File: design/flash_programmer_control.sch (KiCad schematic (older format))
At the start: 10 parts, among them P601 ISP, U601 ATMEGA328P

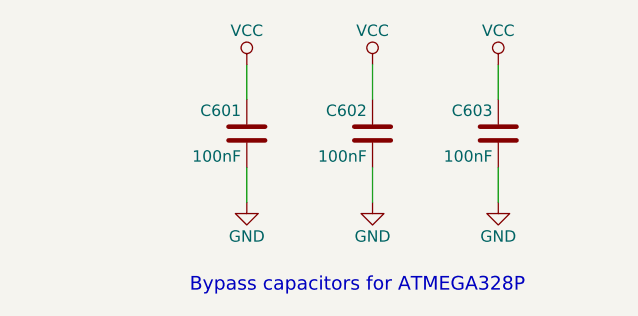
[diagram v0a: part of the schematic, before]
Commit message: Apply license to schematic files
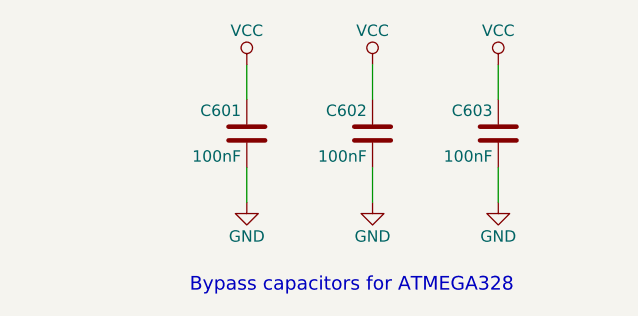
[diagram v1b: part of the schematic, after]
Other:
- note added: "Bypass capacitors for ATMEGA328"
- note removed: "Bypass capacitors for ATMEGA328P"
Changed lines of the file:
@@
 Date "2017-03-11"
 Rev "5"
-Comp "John DiSanti"
+Comp "Copyright 2017 John DiSanti"
 Comment1 ""
 Comment2 ""
@@
 	9500 6100 9500 6250
 Text Notes 8700 6650 0    60   ~ 0
-Bypass capacitors for ATMEGA328P
+Bypass capacitors for ATMEGA328
 $Comp
 L R R601

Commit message: Correction: ATMEGA328P -> ATMEGA328-AU
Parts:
- U601: value ATMEGA328P -> ATMEGA328-AU; symbol ATMEGA328P -> ATMEGA328-AU
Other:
- note added: "Bypass capacitors for ATMEGA328-AU"
- note removed: "Bypass capacitors for ATMEGA328"
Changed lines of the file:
@@
 EESchema Schematic File Version 2
 LIBS:gls27sf010
-LIBS:atmega328p
+LIBS:atmega328au
 LIBS:flash_programmer
 LIBS:power
@@
 	9500 6100 9500 6250
 Text Notes 8700 6650 0    60   ~ 0
-Bypass capacitors for ATMEGA328
+Bypass capacitors for ATMEGA328-AU
 $Comp
 L R R601
@@
 Control
 $Comp
-L ATMEGA328P U?
+L ATMEGA328-AU U?
 U 1 1 58C491ED
 P 3900 3550
@@
 AR Path="/58C243E5/58C491ED" Ref="U601"  Part="1"
 F 0 "U601" H 4100 3800 60  0000 L CNN
-F 1 "ATMEGA328P" H 4100 3700 60  0000 L CNN
+F 1 "ATMEGA328-AU" H 4100 3700 60  0000 L CNN
 F 2 "TQFP_32_7mm_0.8mm_pitch:TQFP-32" H 3900 3550 60  0001 C CNN
 F 3 "" H 3900 3550 60  0001 C CNN
@@
 $EndComp
 $Comp
-L ATMEGA328P U?
+L ATMEGA328-AU U?
 U 2 1 58C4927B
 P 7200 2150
@@
 AR Path="/58C243E5/58C4927B" Ref="U601"  Part="2"
 F 0 "U601" H 7400 2400 60  0000 L CNN
-F 1 "ATMEGA328P" H 7400 2300 60  0000 L CNN
+F 1 "ATMEGA328-AU" H 7400 2300 60  0000 L CNN
 F 2 "TQFP_32_7mm_0.8mm_pitch:TQFP-32" H 7200 2150 60  0001 C CNN
 F 3 "" H 7200 2150 60  0001 C CNN
@@
 $EndComp
 $Comp
-L ATMEGA328P U?
+L ATMEGA328-AU U?
 U 3 1 58C492C6
 P 3900 4200
@@
 AR Path="/58C243E5/58C492C6" Ref="U601"  Part="3"
 F 0 "U601" H 4100 4450 60  0000 L CNN
-F 1 "ATMEGA328P" H 4100 4350 60  0000 L CNN
+F 1 "ATMEGA328-AU" H 4100 4350 60  0000 L CNN
 F 2 "TQFP_32_7mm_0.8mm_pitch:TQFP-32" H 3900 4200 60  0001 C CNN
 F 3 "" H 3900 4200 60  0001 C CNN
@@
 $EndComp
 $Comp
-L ATMEGA328P U?
+L ATMEGA328-AU U?
 U 4 1 58C49325
 P 7200 4100
@@
 AR Path="/58C243E5/58C49325" Ref="U601"  Part="4"
 F 0 "U601" H 7400 4350 60  0000 L CNN
-F 1 "ATMEGA328P" H 7400 4250 60  0000 L CNN
+F 1 "ATMEGA328-AU" H 7400 4250 60  0000 L CNN
 F 2 "TQFP_32_7mm_0.8mm_pitch:TQFP-32" H 7200 4100 60  0001 C CNN
 F 3 "" H 7200 4100 60  0001 C CNN
@@
 $EndComp
 $Comp
-L ATMEGA328P U?
+L ATMEGA328-AU U?
 U 5 1 58C49392
 P 3900 2150
@@
 AR Path="/58C243E5/58C49392" Ref="U601"  Part="5"
 F 0 "U601" H 4100 2400 60  0000 L CNN
-F 1 "ATMEGA328P" H 4100 2300 60  0000 L CNN
+F 1 "ATMEGA328-AU" H 4100 2300 60  0000 L CNN
 F 2 "TQFP_32_7mm_0.8mm_pitch:TQFP-32" H 3900 2150 60  0001 C CNN
 F 3 "" H 3900 2150 60  0001 C CNN
